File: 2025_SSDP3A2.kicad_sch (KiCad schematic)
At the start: 65 parts, among them J1 SolderPad, J2 SolderPad, J3 SolderPad, J4 SolderPad, J5 SolderPad, J6 SolderPad, J7 SolderPad_01x06, Q1 IAUZ30N10S5L240, Q2 BSZ096N10LS5, U1 LM5146RGYR

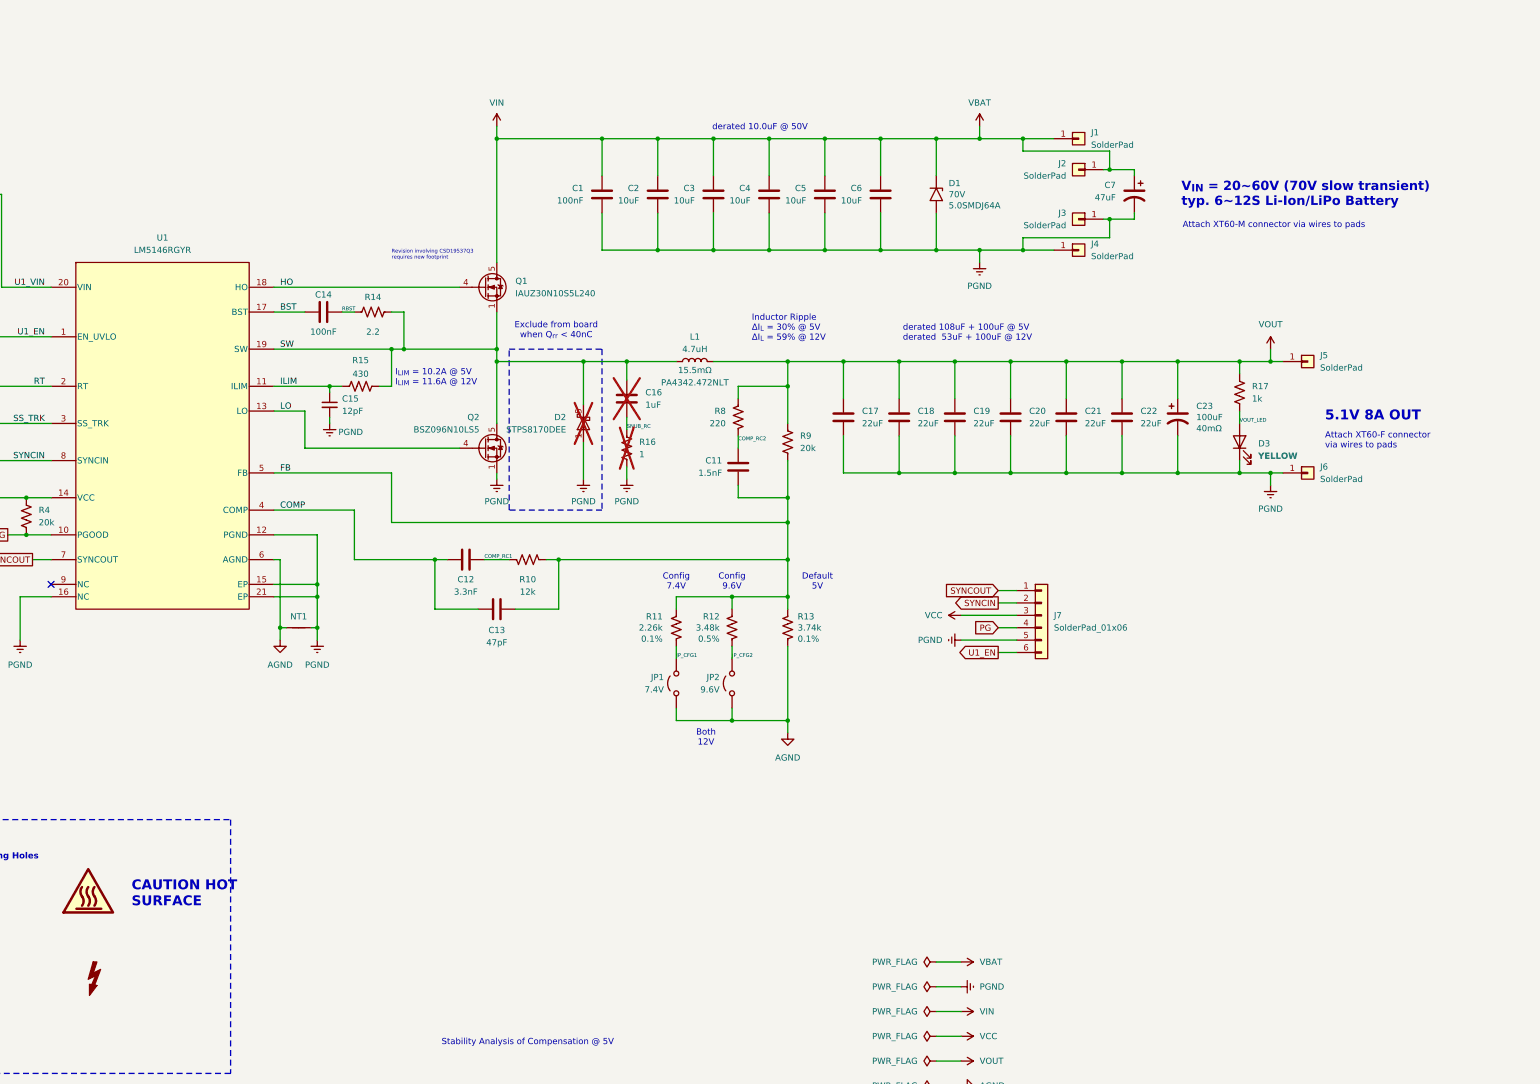
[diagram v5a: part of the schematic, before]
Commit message: Improvements to copper, EMI reduction techniques
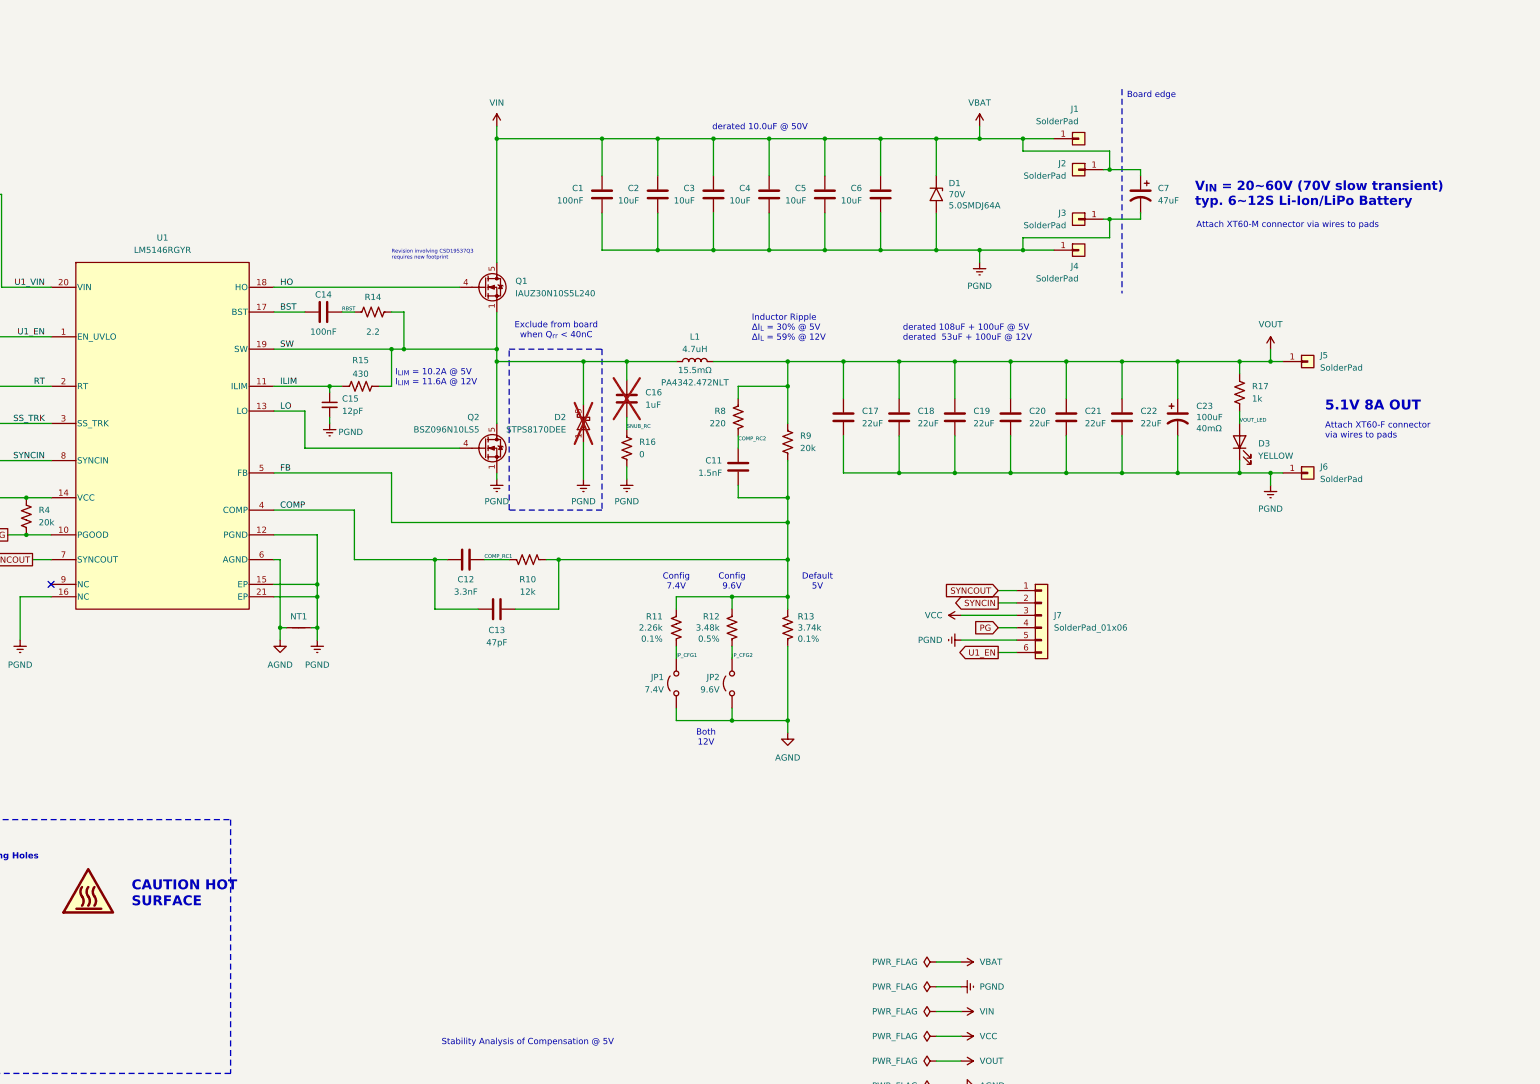
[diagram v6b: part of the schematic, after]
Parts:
- C18, C19, C20, C21, C22: Part Type Basic -> Extended
- D1: LCSC PN C42394454 -> C2990414; Part Type Extended -> Preferred Extended; Power 3000W -> 5000W
- R16: value 1 -> 0; footprint Resistor_SMD:R_1210_3225Metric_Pad1.30x2.65mm_HandSolder -> Resistor_SMD:R_1206_3216Metric_Pad1.30x1.75mm_HandSolder; FT Rotation Offset (none) -> 0; LCSC PN (none) -> C17888; MANUFACTURER (none) -> UNI-ROYAL; Part Type (none) -> Basic; Power (none) -> 0.25W; Tolerance (none) -> 1%; Voltage (none) -> 200V; now fitted; now in the parts list
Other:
- note added: "Board edge"
- moved on the sheet: C7
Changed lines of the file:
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@@
 	(text "V_{IN} = 20~60V (70V slow transient)\ntyp. 6~12S Li-Ion/LiPo Battery"
 		(exclude_from_sim no)
-		(at 329.692 97.79 0)
+		(at 332.486 97.79 0)
 		(effects
 			(font
@@
 	(text "Attach XT60-F connector\nvia wires to pads"
 		(exclude_from_sim no)
-		(at 359.156 148.336 0)
+		(at 359.156 146.304 0)
 		(effects
 			(font
@@
 	(text "Attach XT60-M connector via wires to pads"
 		(exclude_from_sim no)
-		(at 329.946 104.14 0)
+		(at 332.74 104.14 0)
 		(effects
 			(font
@@
 		)
 	)
+	(text "Board edge"
+		(exclude_from_sim no)
+		(at 318.516 77.47 0)
+		(effects
+			(font
+				(size 1.27 1.27)
+			)
+			(justify left)
+		)
+	)
 	(text "FPWM"
 		(exclude_from_sim no)
@@
 	(text "5.1V 8A OUT"
 		(exclude_from_sim no)
-		(at 359.156 143.256 0)
+		(at 359.156 141.224 0)
 		(effects
 			(font
@@
 		)
 	)
+	(polyline
+		(pts
+			(xy 317.5 76.2) (xy 317.5 118.11)
+		)
+		(stroke
+			(width 0.1778)
+			(type dash)
+		)
+	)
 	(wire
 		(pts
@@
 	(wire
 		(pts
-			(xy 320.04 92.71) (xy 314.96 92.71)
+			(xy 321.31 92.71) (xy 314.96 92.71)
 		)
 		(stroke
@@
 	(wire
 		(pts
-			(xy 320.04 101.6) (xy 320.04 102.87)
+			(xy 321.31 101.6) (xy 321.31 102.87)
 		)
 		(stroke
@@
 	(wire
 		(pts
-			(xy 320.04 92.71) (xy 320.04 93.98)
+			(xy 321.31 92.71) (xy 321.31 93.98)
 		)
 		(stroke
@@
 	(wire
 		(pts
-			(xy 320.04 102.87) (xy 314.96 102.87)
+			(xy 321.31 102.87) (xy 314.96 102.87)
 		)
 		(stroke
@@
 		(on_board yes)
 		(dnp no)
-		(fields_autoplaced yes)
 		(property "Reference" "J1"
-			(at 311.15 85.09 0)
+			(at 308.61 80.264 0)
 			(effects
 				(font
 					(size 1.27 1.27)
 				)
-				(justify left)
+				(justify right)
 			)
 		)
 		(property "Value" "SolderPad"
-			(at 311.15 87.63 0)
+			(at 308.61 82.804 0)
 			(effects
 				(font
 					(size 1.27 1.27)
 				)
-				(justify left)
+				(justify right)
 			)
 		)
@@
 		(on_board yes)
 		(dnp no)
-		(fields_autoplaced yes)
 		(property "Reference" "J4"
-			(at 311.15 107.95 0)
+			(at 308.61 112.522 0)
 			(effects
 				(font
 					(size 1.27 1.27)
 				)
-				(justify left)
+				(justify right)
 			)
 		)
 		(property "Value" "SolderPad"
-			(at 311.15 110.49 0)
+			(at 308.61 115.062 0)
 			(effects
 				(font
 					(size 1.27 1.27)
 				)
-				(justify left)
+				(justify right)
 			)
 		)
@@
 	(symbol
 		(lib_id "Device:C_Polarized_US")
-		(at 320.04 97.79 0)
+		(at 321.31 97.79 0)
 		(mirror y)
 		(unit 1)
@@
 		(on_board no)
 		(dnp no)
-		(fields_autoplaced yes)
 		(property "Reference" "C7"
-			(at 316.23 95.885 0)
+			(at 324.866 96.52 0)
 			(effects
 				(font
 					(size 1.27 1.27)
 				)
-				(justify left)
+				(justify right)
 			)
 		)
 		(property "Value" "47uF"
-			(at 316.23 98.425 0)
+			(at 324.866 99.06 0)
 			(effects
 				(font
 					(size 1.27 1.27)
 				)
-				(justify left)
+				(justify right)
 			)
 		)
 		(property "Footprint" ""
-			(at 320.04 97.79 0)
+			(at 321.31 97.79 0)
 			(effects
 				(font
@@
 		)
 		(property "Datasheet" "~"
-			(at 320.04 97.79 0)
+			(at 321.31 97.79 0)
 			(effects
 				(font
@@
 		)
 		(property "Description" "Polarized capacitor, US symbol"
-			(at 320.04 97.79 0)
+			(at 321.31 97.79 0)
 			(effects
 				(font
@@
 		(unit 1)
 		(exclude_from_sim no)
-		(in_bom no)
+		(in_bom yes)
 		(on_board yes)
-		(dnp yes)
+		(dnp no)
 		(fields_autoplaced yes)
 		(property "Reference" "R16"
@@
 			)
 		)
-		(property "Value" "1"
+		(property "Value" "0"
 			(at 218.44 151.13 0)
 			(effects
@@
 			)
 		)
-		(property "Footprint" "Resistor_SMD:R_1210_3225Metric_Pad1.30x2.65mm_HandSolder"
+		(property "Footprint" "Resistor_SMD:R_1206_3216Metric_Pad1.30x1.75mm_HandSolder"
 			(at 216.916 150.114 90)
 			(effects
@@
 			)
 		)
-		(property "Description" "Resistor, US symbol"
+		(property "Description" "1206W4F0000T5E"
+			(at 215.9 149.86 0)
+			(effects
+				(font
+					(size 1.27 1.27)
+				)
+				(hide yes)
+			)
+		)
+		(property "FT Rotation Offset" "0"
+			(at 215.9 149.86 0)
+			(effects
+				(font
+					(size 1.27 1.27)
+				)
+				(hide yes)
+			)
+		)
+		(property "LCSC PN" "C17888"
+			(at 215.9 149.86 0)
+			(effects
+				(font
+					(size 1.27 1.27)
+				)
+				(hide yes)
+			)
+		)
+		(property "MANUFACTURER" "UNI-ROYAL"
+			(at 215.9 149.86 0)
+			(effects
+				(font
+					(size 1.27 1.27)
+				)
+				(hide yes)
+			)
+		)
+		(property "Part Type" "Basic"
+			(at 215.9 149.86 0)
+			(effects
+				(font
+					(size 1.27 1.27)
+				)
+				(hide yes)
+			)
+		)
+		(property "Power" "0.25W"
+			(at 215.9 149.86 0)
+			(effects
+				(font
+					(size 1.27 1.27)
+				)
+				(hide yes)
+			)
+		)
+		(property "Tolerance" "1%"
+			(at 215.9 149.86 0)
+			(effects
+				(font
+					(size 1.27 1.27)
+				)
+				(hide yes)
+			)
+		)
+		(property "Voltage" "200V"
 			(at 215.9 149.86 0)
 			(effects
@@
 			)
 		)
-		(property "Part Type" "Basic"
+		(property "Part Type" "Extended"
 			(at 306.07 143.51 0)
 			(effects
@@
 	)
 	(symbol
-		(lib_id "Graphic:SYM_Flash_Small")
-		(at 106.68 259.08 0)
-		(unit 1)
-		(exclude_from_sim yes)
-		(in_bom no)
-		(on_board no)
-		(dnp no)
-		(fields_autoplaced yes)
-		(property "Reference" "#SYM2"
-			(at 104.394 259.08 90)
-			(effects
-				(font
-					(size 1.27 1.27)
-				)
-				(hide yes)
-			)
-		)
-		(property "Value" "SYM_Flash_Small"
-			(at 108.966 259.08 90)
-			(effects
-				(font
-					(size 1.27 1.27)
-				)
-				(hide yes)
-			)
-		)
-		(property "Footprint" "Symbol:Symbol_HighVoltage_NoTriangle_2x5mm_Copper"
-			(at 106.68 259.715 0)
-			(effects
-				(font
-					(size 1.27 1.27)
-				)
-				(hide yes)
-			)
-		)
-		(property "Datasheet" "~"
-			(at 116.84 261.62 0)
-			(effects
-				(font
-					(size 1.27 1.27)
-				)
-				(hide yes)
-			)
-		)
-		(property "Description" "Flash symbol, small"
-			(at 106.68 259.08 0)
-			(effects
-				(font
-					(size 1.27 1.27)
-				)
-				(hide yes)
-			)
-		)
-		(instances
-			(project ""
-				(path "/ea689c3b-fea3-4fc0-9d65-1fb672b240d8"
-					(reference "#SYM2")
-					(unit 1)
-				)
-			)
-		)
-	)
-	(symbol
 		(lib_id "power:GND")
 		(at 53.34 189.23 0)
@@
 				(font
 					(size 1.27 1.27)
-					(thickness 0.254)
-					(bold yes)
-					(color 194 194 0 1)
+					(thickness 0.1588)
 				)
 				(justify right)
@@
 			)
 		)
-		(property "Part Type" "Basic"
+		(property "Part Type" "Extended"
 			(at 271.78 143.51 0)
 			(effects
@@
 			)
 		)
-		(property "Part Type" "Basic"
+		(property "Part Type" "Extended"
 			(at 283.21 143.51 0)
 			(effects
@@
 			)
 		)
-		(property "Part Type" "Basic"
+		(property "Part Type" "Extended"
 			(at 317.5 143.51 0)
 			(effects
@@
 			)
 		)
-		(property "Part Type" "Basic"
+		(property "Part Type" "Extended"
 			(at 294.64 143.51 0)
 			(effects
@@
 			)
 		)
-		(property "Datasheet" "https://jlcpcb.com/api/file/downloadByFileSystemAccessId/8564879186138451968"
+		(property "Datasheet" "https://jlcpcb.com/api/file/downloadByFileSystemAccessId/8589837529181548544"
 			(at 279.4 97.79 0)
 			(effects
@@
 			)
 		)
-		(property "LCSC PN" "C42394454"
+		(property "LCSC PN" "C2990414"
 			(at 279.4 97.79 90)
 			(effects
@@
 			)
 		)
-		(property "Part Type" "Extended"
+		(property "Part Type" "Preferred Extended"
 			(at 279.4 97.79 90)
 			(effects
@@
 			)
 		)
-		(property "Power" "3000W"
+		(property "Power" "5000W"
 			(at 279.4 97.79 90)
 			(effects

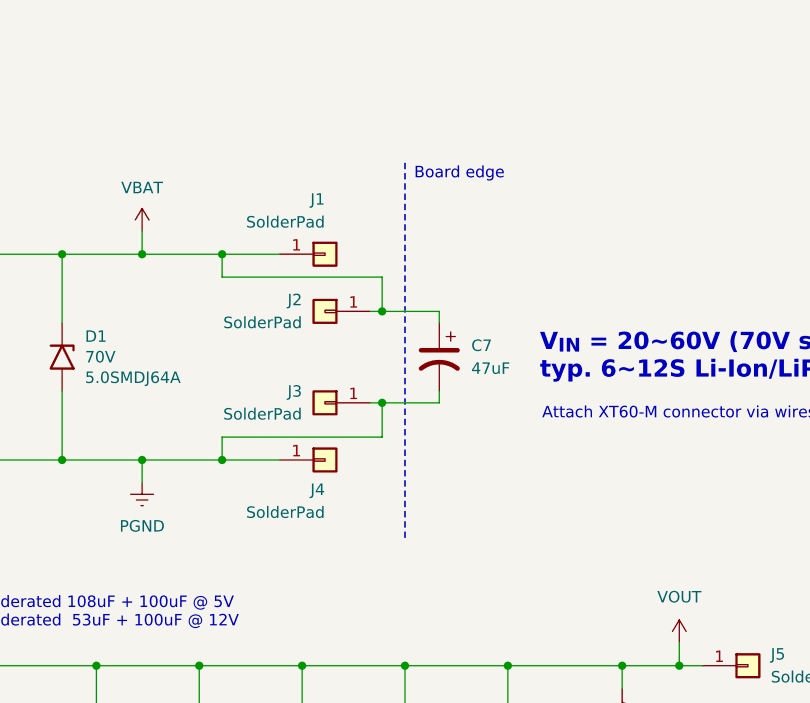
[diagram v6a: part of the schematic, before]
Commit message: Updated schematic, added more silkscreen markings
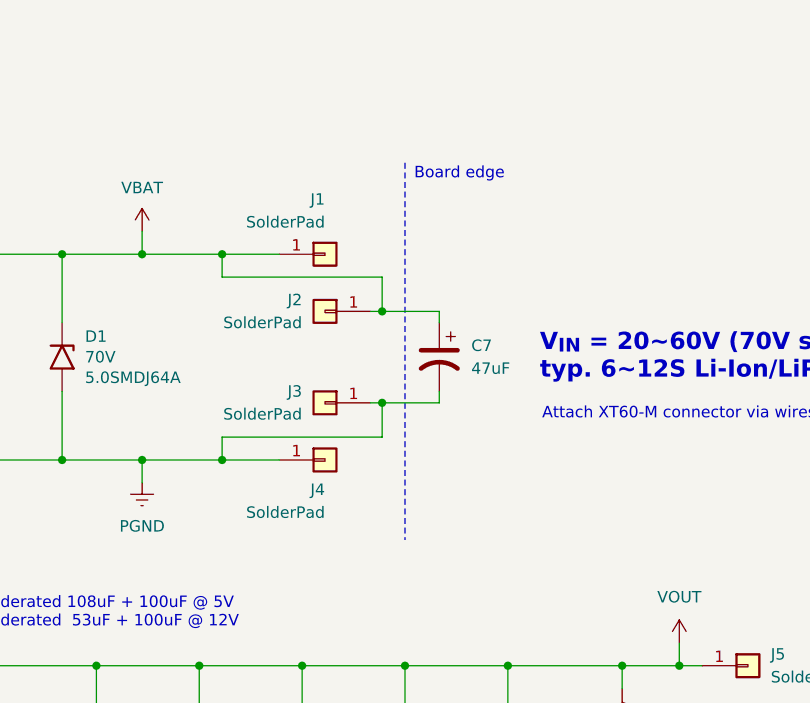
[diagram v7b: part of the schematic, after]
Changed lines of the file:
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@@
 		)
 		(stroke
-			(width 0.1778)
+			(width 0)
 			(type dash)
 		)

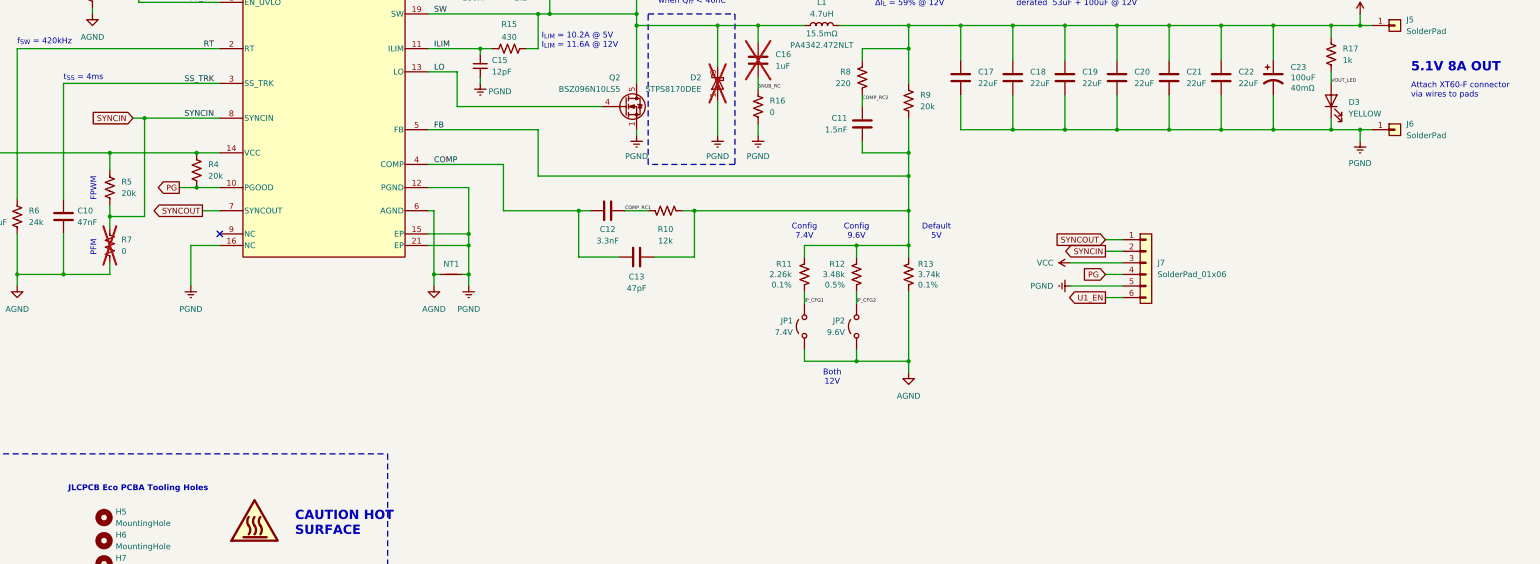
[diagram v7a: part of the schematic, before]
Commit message: Added TVS protection to aux IO
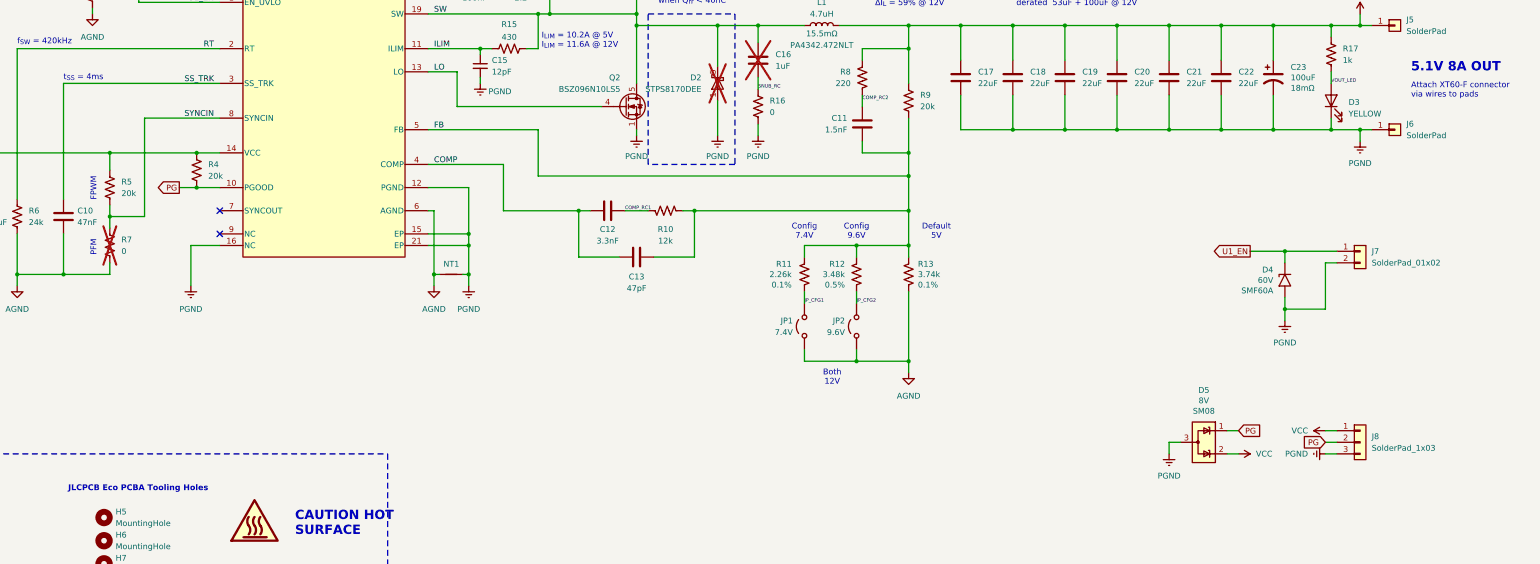
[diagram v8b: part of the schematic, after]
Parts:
- removed J7: SolderPad_01x06, Connector_Custom:SolderWirePad_1x06_SMD_1.5x2mm, symbol Connector_Generic:Conn_01x06
- added D4: 60V, Diode_SMD:D_SMF, symbol Diode:SMF58A
- added D5: 8V, Package_TO_SOT_SMD:SOT-23-3, symbol Power_Protection:ESDA5V3L
- added J7: SolderPad_01x02, Connector_Custom:SolderWirePad_1x02_SMD_1.5x2mm, symbol Connector_Generic:Conn_01x02
- added J8: SolderPad_1x03, Connector_Custom:SolderWirePad_1x03_SMD_1.5x2mm, symbol Connector_Generic:Conn_01x03
- C23: ESR 40mΩ -> 18mΩ
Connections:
- net PG: now also D5.1 (K), J8.2 (Pin_2)
- net PGND: now also D4.2 (A2), D5.3 (A), J7.2 (Pin_2), J8.3 (Pin_3)
- net U1_EN: now also D4.1 (A1), J7.1 (Pin_1)
- net VCC: now also D5.2 (K), J8.1 (Pin_1)
- net SYNCOUT: no longer names the net of U1.7 (SYNCOUT)
- no-connect marks 1 -> 2
